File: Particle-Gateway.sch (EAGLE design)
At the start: 24 parts, among them J2 GROVE-I2C, J3 Lipo Battery, J4 GROVE-I2C, J5 CON_HEADER_1X08-PTH, P1 PADSMALL, U1 AMS1117-3.3

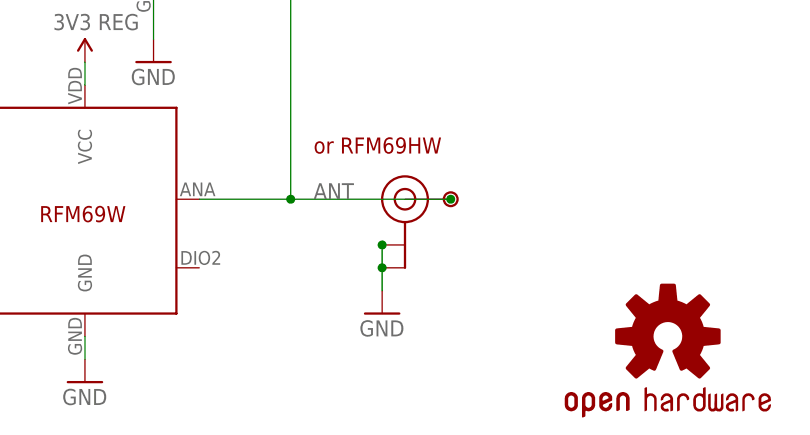
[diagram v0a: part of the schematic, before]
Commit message: Adjusted SMA connector exposed PAD
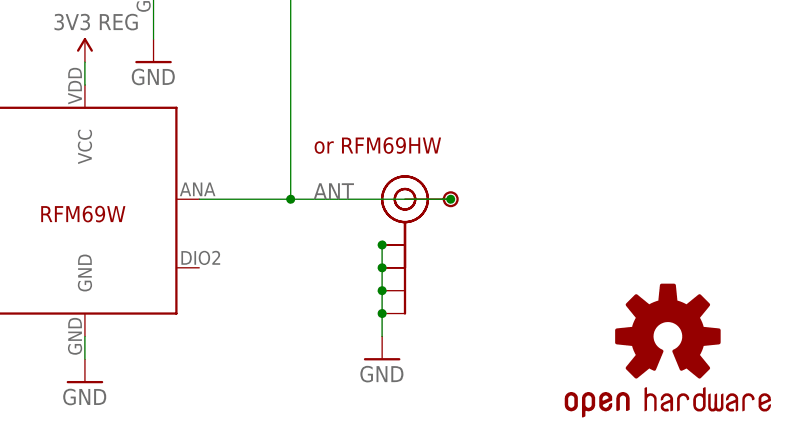
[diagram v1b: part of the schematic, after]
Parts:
- added J$1: SMA_EDGE, SparkFun-Connectors:SMA_EDGE
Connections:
- net ANT: now also J$1.SIGNAL
- net GND: now also J$1.GND@0, J$1.GND@1, J$1.GND@2, J$1.GND@3
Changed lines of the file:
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@@
 <?xml version="1.0" encoding="utf-8"?>
 <!DOCTYPE eagle SYSTEM "eagle.dtd">
-<eagle version="6.6.0">
+<eagle version="7.3.0">
 <drawing>
 <settings>
@@
 <setting verticaltext="up"/>
 </settings>
-<grid distance="50" unitdist="mil" unit="mil" style="lines" multiple="1" display="yes" altdistance="5" altunitdist="mil" altunit="mil"/>
+<grid distance="0.1" unitdist="inch" unit="inch" style="lines" multiple="1" display="no" altdistance="0.01" altunitdist="inch" altunit="inch"/>
 <layers>
 <layer number="1" name="Top" color="4" fill="1" visible="no" active="no"/>
@@
 <part name="J2" library="seeed-opl-Connector" deviceset="GROVE-4P-2.0" device="-3470140P1" value="GROVE-I2C"/>
 <part name="NAME" library="SparkFun-Aesthetics" deviceset="FRAME-A4L" device="" value="Value">
-<attribute name="CNAME" value="Spark RF Gateway + Display"/>
-<attribute name="CREVISION" value="1.0"/>
+<attribute name="CNAME" value="Particle RF Gateway + Display"/>
+<attribute name="CREVISION" value="1.0a"/>
 <attribute name="DESIGNER" value="Charles-Henri Hallard"/>
 </part>
@@
 <part name="3V3CORE" library="Seeed-Discrete" deviceset="PAD-JUMPER-2P" device=""/>
 <part name="5VFTDI" library="Seeed-Discrete" deviceset="PAD-JUMPER-2P" device=""/>
+<part name="J$1" library="SparkFun-Connectors" deviceset="SMA_EDGE" device=""/>
 </parts>
 <sheets>
@@
 <instance part="P1" gate="G$1" x="147.32" y="30.48"/>
 <instance part="U-FL" gate="G$1" x="142.24" y="30.48"/>
-<instance part="GND9" gate="1" x="139.7" y="17.78"/>
+<instance part="GND9" gate="1" x="139.7" y="12.7"/>
 <instance part="GND1" gate="1" x="106.68" y="10.16"/>
 <instance part="GND13" gate="1" x="30.48" y="15.24"/>
@@
 <attribute name="NAME" x="160.274" y="115.062" size="1.27" layer="95" ratio="10" rot="R180"/>
 </instance>
+<instance part="J$1" gate="1" x="142.24" y="30.48"/>
 </instances>
 <busses>
@@
 <wire x1="139.7" y1="22.86" x2="139.7" y2="20.32" width="0.1524" layer="91"/>
 <junction x="139.7" y="25.4"/>
+<pinref part="J$1" gate="1" pin="GND@0"/>
+<pinref part="J$1" gate="1" pin="GND@1"/>
+<pinref part="J$1" gate="1" pin="GND@2"/>
+<wire x1="139.7" y1="20.32" x2="139.7" y2="17.78" width="0.1524" layer="91"/>
+<junction x="139.7" y="20.32"/>
+<pinref part="J$1" gate="1" pin="GND@3"/>
+<wire x1="139.7" y1="17.78" x2="139.7" y2="15.24" width="0.1524" layer="91"/>
+<junction x="139.7" y="17.78"/>
 </segment>
 <segment>
@@
 <pinref part="U-FL" gate="G$1" pin="SIGNAL"/>
 <junction x="147.32" y="30.48"/>
-</segment>
-</net>
+<pinref part="J$1" gate="1" pin="SIGNAL"/>
+</segment>
+</net>
